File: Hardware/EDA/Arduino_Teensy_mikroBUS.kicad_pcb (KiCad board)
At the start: 4 copper layers, 38.1 x 69.8 mm, 32 parts, among them J1 HEADER_F_2.54MM_1R8P_ST_AU_PTH, J2 HEADER_F_2.54MM_1R8P_ST_AU_PTH, J3 HEADER_F_2.54MM_1R11P_ST_AU_P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, J3 Val**, J4 HEADER_F_2.54MM_1R11P_ST_AU_P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, J4 Val**, J5 Molex_0475710001, M1 FID, M2 FID, M3 FID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

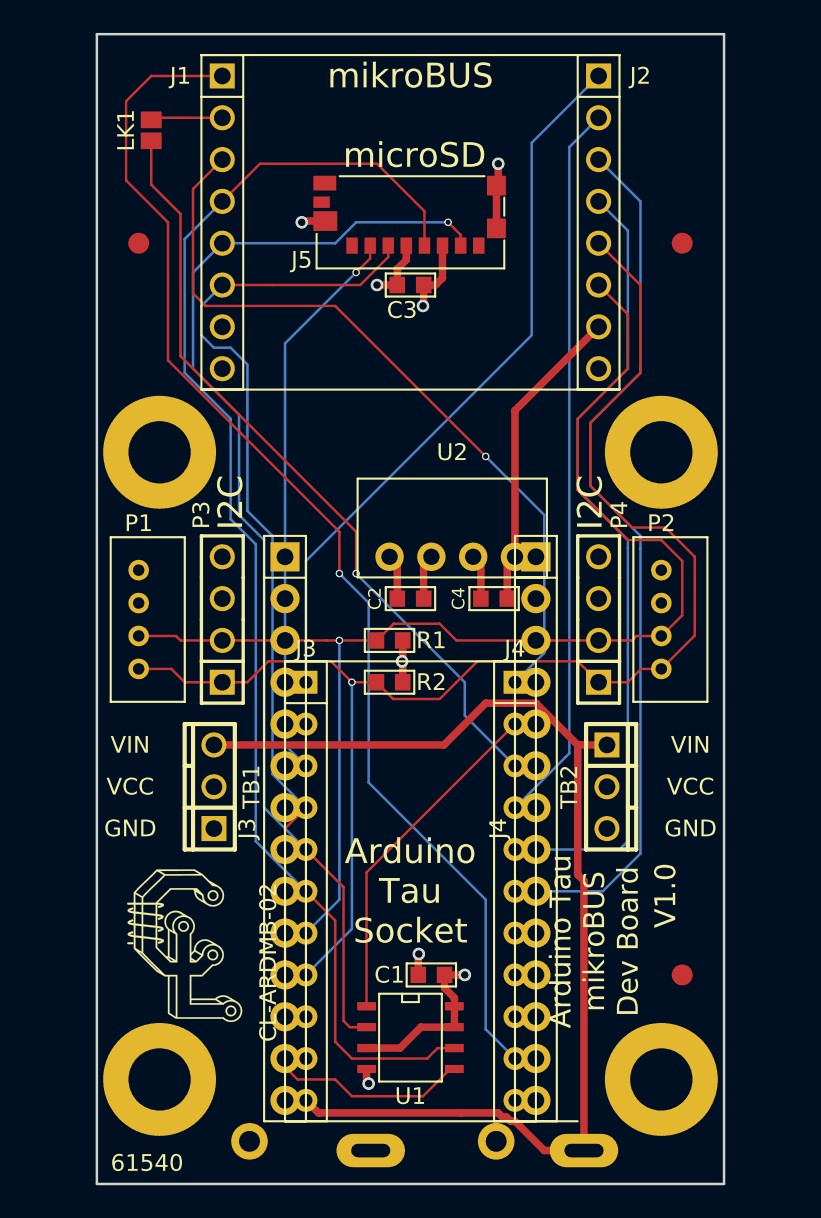
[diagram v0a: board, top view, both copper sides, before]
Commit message: Updated schematic, netlist and read in netlist to PCB file.  Added pinouts for Teensy.
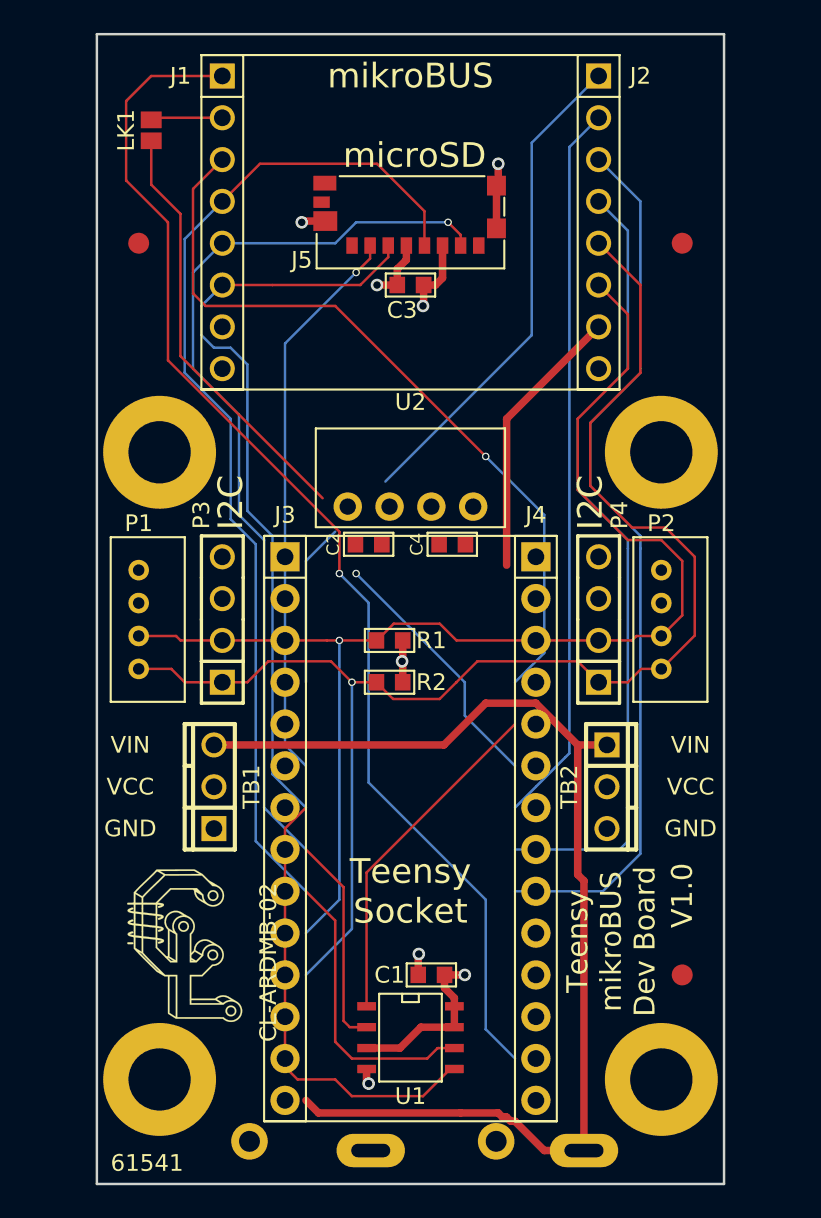
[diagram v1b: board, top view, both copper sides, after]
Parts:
- removed the J3 at (73.7, 83.8)
- removed the J4 at (86.4, 83.8)
- J3, J4: value Val** -> HEADER_F_2.54MM_1R14P_ST_AU_PTH
- moved C2 4.17 mm to (77.5, 62.7)
- moved C4 4.17 mm to (82.5, 62.7)
- moved U2 3.97 mm to (80.0, 60.5)
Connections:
- J2 pad 3: RXD -> RX1
- J2 pad 4: TXD -> TX1
- J3 pad 1: (no net) -> SCK
- J3 pad 10: (no net) -> A8
- J3 pad 11: (no net) -> A9
- J3 pad 12: (no net) -> 3V3
- J3 pad 13: (no net) -> GND
- J3 pad 14: (no net) -> VIN
- J3 pad 2: (no net) -> A0
- J3 pad 3: (no net) -> A1
- J3 pad 4: (no net) -> A2
- J3 pad 5: (no net) -> A3
- J3 pad 6: (no net) -> SDA
- J3 pad 7: (no net) -> SCL
- J3 pad 8: (no net) -> A6
- J3 pad 9: (no net) -> A7
- J4 pad 1: (no net) -> MISO
- J4 pad 10: (no net) -> D3
- J4 pad 11: (no net) -> D2
- J4 pad 12: (no net) -> TX1
- J4 pad 13: (no net) -> RX1
- J4 pad 14: (no net) -> GND
- J4 pad 2: (no net) -> MOSI
- J4 pad 3: (no net) -> D10
- J4 pad 4: (no net) -> D9
- J4 pad 5: (no net) -> D8
- J4 pad 6: (no net) -> D7
- J4 pad 7: (no net) -> D6
- J4 pad 8: (no net) -> D5
- J4 pad 9: (no net) -> D4
- J5 pad 1: (no net) -> Net-(J5-Pad1)
- J5 pad 12: (no net) -> Net-(J5-Pad12)
- J5 pad 13: (no net) -> Net-(J5-Pad13)
- J5 pad 2: D10 -> D6
- J5 pad 8: (no net) -> Net-(J5-Pad8)
- M1 pad ~: (no net) -> Net-(M1-Pad~)
- M2 pad ~: (no net) -> Net-(M2-Pad~)
- M3 pad ~: (no net) -> Net-(M3-Pad~)
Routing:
- net RXD: track 54.3 -> 0.00 mm
- net RX1: track 0.00 -> 54.3 mm
- net TXD: track 49.2 -> 0.00 mm
- net TX1: track 0.00 -> 49.2 mm
- net D6: track 0.00 -> 34.3 mm, vias 0 -> 1
- net D10: track 34.3 -> 0.00 mm, vias 1 -> 0
- net (no net): track 0.00 -> 25.6 mm, vias 0 -> 1
- net MOSI: track 75.0 -> 49.6 mm
- net D3: track 47.1 -> 26.0 mm, vias 1 -> 0
- net GND: track 17.7 -> 37.7 mm
- net D8: track 44.2 -> 30.0 mm
- net 3V3: track 19.7 -> 16.9 mm
- net 5.0V: track 18.8 -> 16.8 mm
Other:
- board text added: "61541"
- board text added: "Teensy Socket"
- board text added: "Teensy mikroBUS Dev Board"
- board text removed: "61540"
- board text removed: "Arduino Tau Socket"
- board text removed: "Arduino Tau mikroBUS Dev Board"

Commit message: Completed PCB layout, added PCB render image, generated gerbers and schematic.
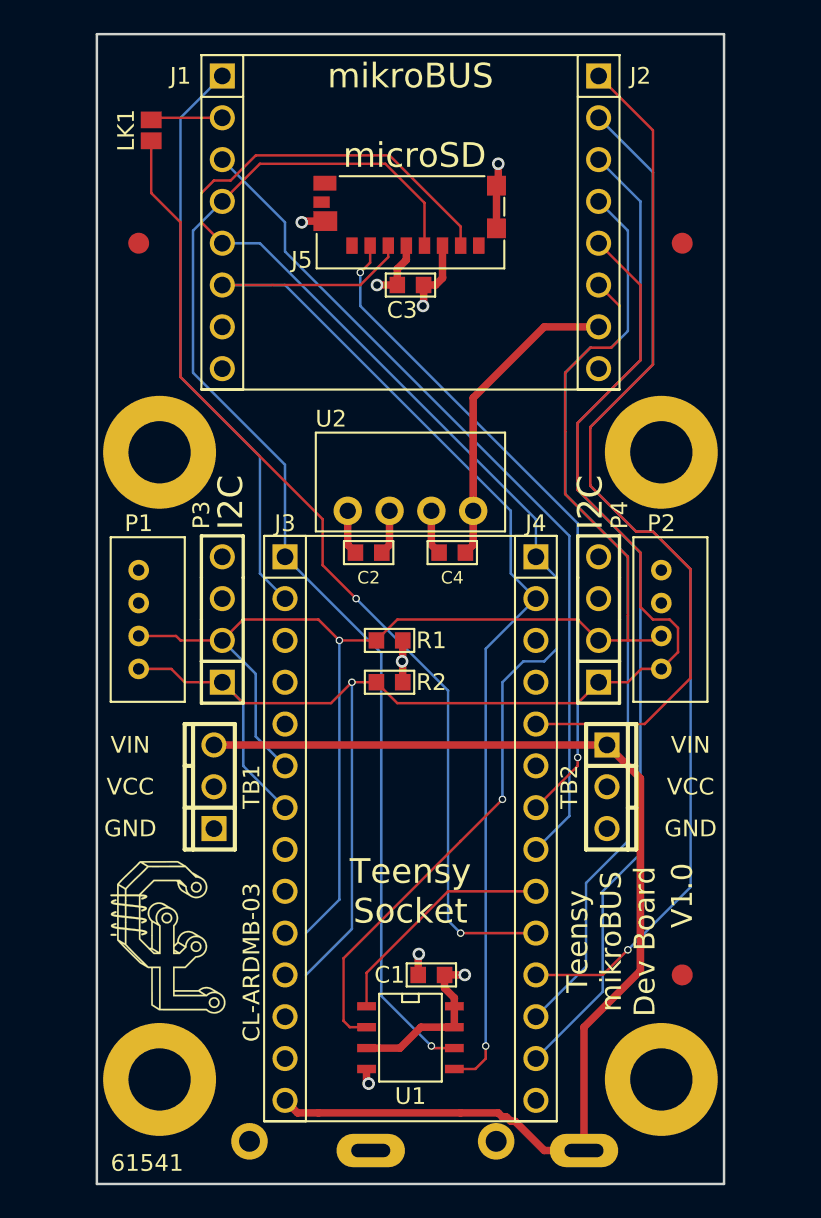
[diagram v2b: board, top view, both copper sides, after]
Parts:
- moved G1 1.14 mm to (65.3, 86.6)
- moved C2 0.51 mm to (77.5, 63.2)
- moved C4 0.51 mm to (82.5, 63.2)
- moved U2 0.25 mm to (80.0, 60.7)
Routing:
- net A0: track 74.4 -> 35.4 mm, vias 1 -> 0
- net D3: track 26.0 -> 60.5 mm, vias 0 -> 2
- net (no net): track 25.6 -> 0.00 mm, vias 1 -> 0
- net D8: track 30.0 -> 53.2 mm
- net MOSI: track 49.6 -> 72.3 mm, vias 0 -> 1
- net D2: track 44.0 -> 64.4 mm, vias 0 -> 1
- net GND: track 37.7 -> 17.7 mm
- net MISO: track 69.8 -> 88.4 mm
- net SDA: track 79.1 -> 87.7 mm
- net SCL: track 87.1 -> 94.7 mm
- net TX1: track 49.2 -> 56.5 mm
- net RX1: track 54.3 -> 61.4 mm
- net D6: track 34.3 -> 40.9 mm, vias 1 -> 2
- net D4: track 20.9 -> 14.4 mm
- net D5: track 46.7 -> 51.5 mm, vias 1 -> 0
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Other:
- board text added: "CL-ARDMB-03"
- board text removed: "CL-ARDMB-02"

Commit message: Changed PCB outline/size to accomodate mounting holes, but still fit in enclosure. Regenerated Gerbers and PCB render images.
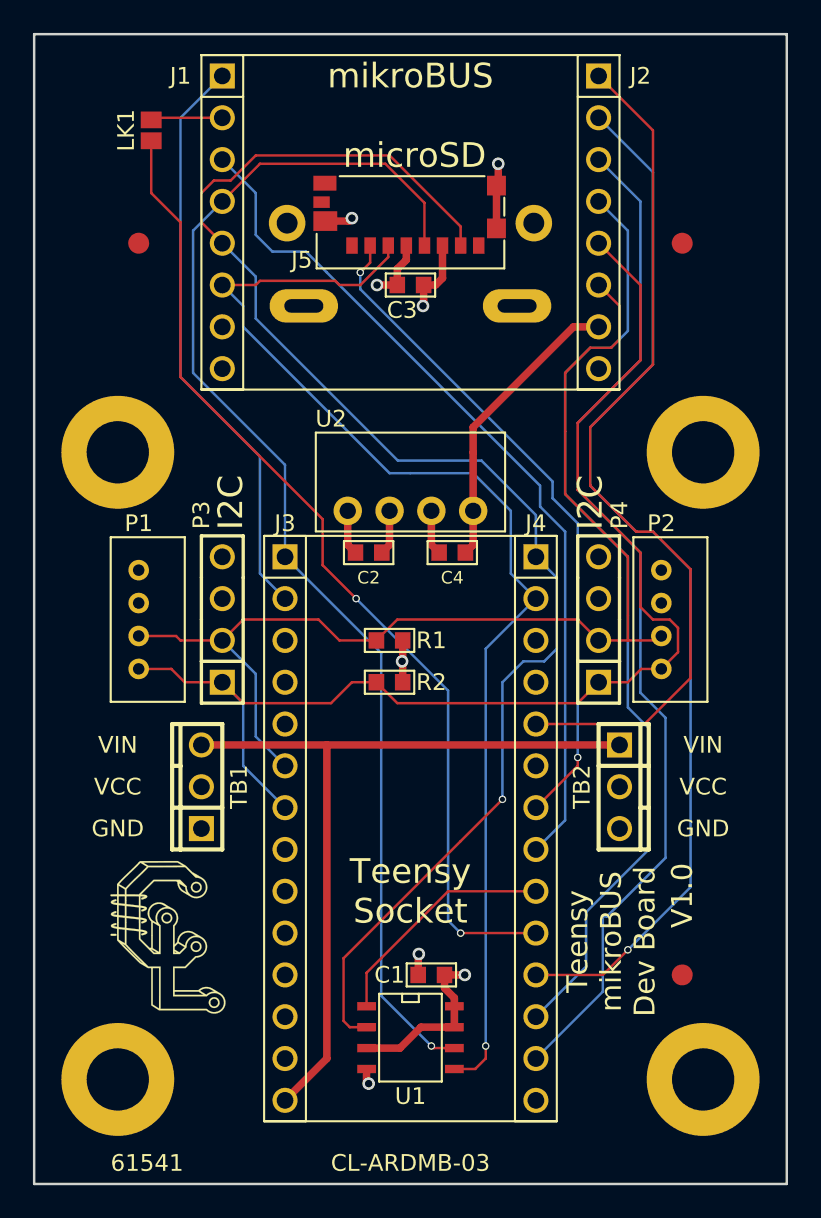
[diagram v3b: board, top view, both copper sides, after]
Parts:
- moved B1 51.5 mm to (80.0, 48.3), turned to 270 degrees
- moved MH2 2.54 mm to (97.8, 57.1)
- moved MH4 2.54 mm to (97.8, 95.2)
- moved MH1 2.54 mm to (62.2, 57.1)
- moved MH3 2.54 mm to (62.2, 95.2)
- moved B2 2.29 mm to (80.0, 71.1), turned to 90 degrees
- moved TB1 0.76 mm to (67.3, 77.5)
- moved TB2 0.76 mm to (92.7, 77.5)
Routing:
- net SCL: track 94.7 -> 75.8 mm, vias 1 -> 0
- net SDA: track 87.7 -> 69.1 mm, vias 1 -> 0
- net VIN: track 70.2 -> 77.3 mm
- net MISO: track 88.4 -> 90.0 mm
- net RX1: track 61.4 -> 62.9 mm
- net TX1: track 56.5 -> 57.5 mm
- net 5.0V: track 19.0 -> 18.0 mm
- net D5: track 51.5 -> 52.5 mm
- net MOSI: track 72.3 -> 73.2 mm
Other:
- board size 38.1 x 69.8 mm -> 45.7 x 69.8 mm

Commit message: Adjustment of mounting hole locations was missed. Corrected and updated gerbers and dimensions.
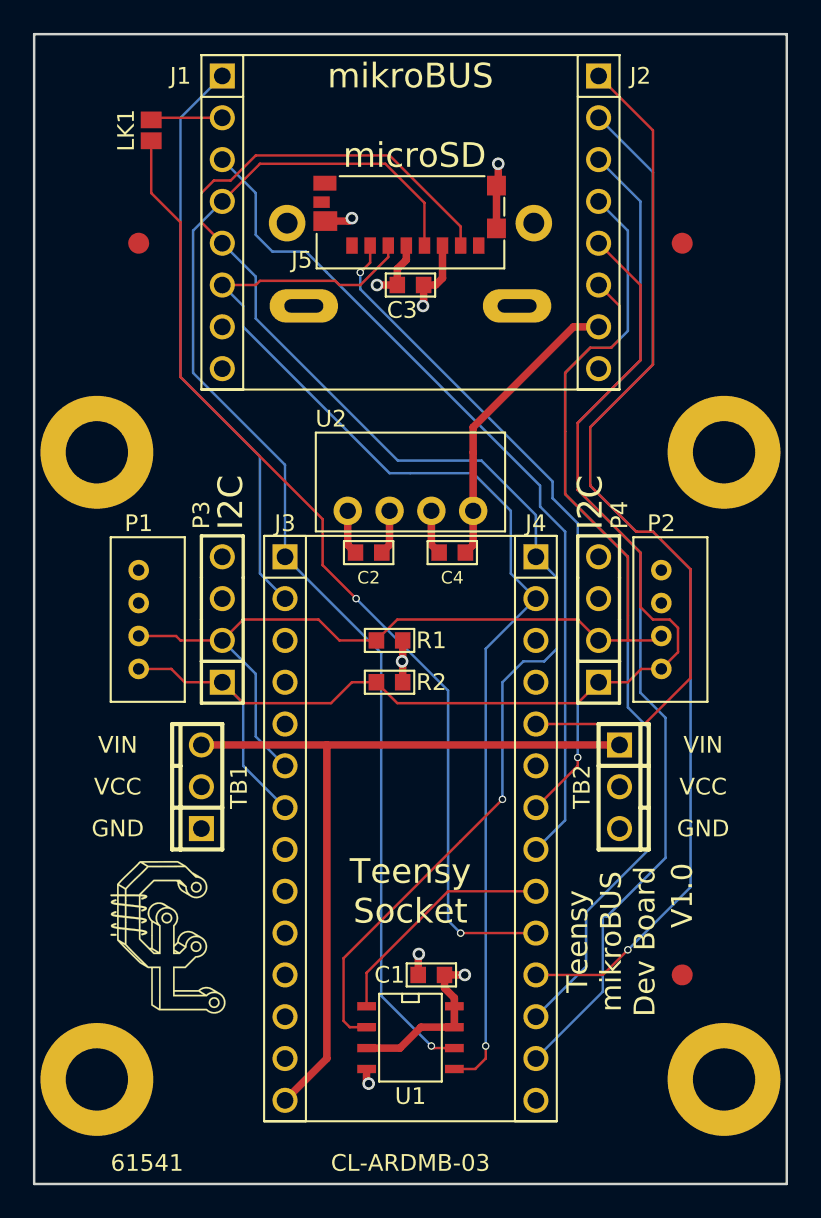
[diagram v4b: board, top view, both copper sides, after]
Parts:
- moved MH1 1.27 mm to (61.0, 57.1)
- moved MH2 1.27 mm to (99.1, 57.1)
- moved MH3 1.27 mm to (61.0, 95.2)
- moved MH4 1.27 mm to (99.1, 95.2)
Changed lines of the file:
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@@
       (net 36 "Net-(M3-Pad~)") (solder_mask_margin 0.635) (clearance 0.635))
   )
-  (module Fastener:MH_#6 (layer F.Cu)
-    (at 62.23 57.15)
+  (module Fastener:MH_#6 locked (layer F.Cu)
+    (at 60.96 57.15)
     (fp_text reference MH1 (at 0 4.445) (layer F.SilkS) hide
       (effects (font (size 1 1) (thickness 0.15)))
@@
       (net 1 GND))
   )
-  (module Fastener:MH_#6 (layer F.Cu)
-    (at 97.79 57.15)
+  (module Fastener:MH_#6 locked (layer F.Cu)
+    (at 99.06 57.15)
     (fp_text reference MH2 (at 0 4.445) (layer F.SilkS) hide
       (effects (font (size 1 1) (thickness 0.15)))
@@
       (net 1 GND))
   )
-  (module Fastener:MH_#6 (layer F.Cu)
-    (at 62.23 95.25)
+  (module Fastener:MH_#6 locked (layer F.Cu)
+    (at 60.96 95.25)
     (fp_text reference MH3 (at -1.524 -4.318) (layer F.SilkS) hide
       (effects (font (size 1 1) (thickness 0.15)))
@@
       (net 1 GND))
   )
-  (module Fastener:MH_#6 (layer F.Cu)
-    (at 97.79 95.25)
+  (module Fastener:MH_#6 locked (layer F.Cu)
+    (at 99.06 95.25)
     (fp_text reference MH4 (at 1.778 -4.318) (layer F.SilkS) hide
       (effects (font (size 1 1) (thickness 0.15)))
@@
     )
   )
+  (dimension 41.91 (width 0.3) (layer Dwgs.User)
+    (gr_text "1.6500 in" (at 78.105 111.84) (layer Dwgs.User)
+      (effects (font (size 1.5 1.5) (thickness 0.3)))
+    )
+    (feature1 (pts (xy 99.06 102.87) (xy 99.06 113.19)))
+    (feature2 (pts (xy 57.15 102.87) (xy 57.15 113.19)))
+    (crossbar (pts (xy 57.15 110.49) (xy 99.06 110.49)))
+    (arrow1a (pts (xy 99.06 110.49) (xy 97.933496 111.076421)))
+    (arrow1b (pts (xy 99.06 110.49) (xy 97.933496 109.903579)))
+    (arrow2a (pts (xy 57.15 110.49) (xy 58.276504 111.076421)))
+    (arrow2b (pts (xy 57.15 110.49) (xy 58.276504 109.903579)))
+  )
+  (dimension 3.81 (width 0.3) (layer Dwgs.User)
+    (gr_text "0.1500 in" (at 67.31 105.41) (layer Dwgs.User)
+      (effects (font (size 1.5 1.5) (thickness 0.3)))
+    )
+    (feature1 (pts (xy 60.96 102.87) (xy 60.96 108.11)))
+    (feature2 (pts (xy 57.15 102.87) (xy 57.15 108.11)))
+    (crossbar (pts (xy 57.15 105.41) (xy 60.96 105.41)))
+    (arrow1a (pts (xy 60.96 105.41) (xy 59.833496 105.996421)))
+    (arrow1b (pts (xy 60.96 105.41) (xy 59.833496 104.823579)))
+    (arrow2a (pts (xy 57.15 105.41) (xy 58.276504 105.996421)))
+    (arrow2b (pts (xy 57.15 105.41) (xy 58.276504 104.823579)))
+  )
   (dimension 45.72 (width 0.3) (layer Dwgs.User)
     (gr_text "1.8000 in" (at 80.01 26.59) (layer Dwgs.User)
@@
   (gr_line (start 57.15 31.75) (end 102.87 31.75) (angle 90) (layer Edge.Cuts) (width 0.15))
   (gr_line (start 57.15 101.6) (end 102.87 101.6) (angle 90) (layer Edge.Cuts) (width 0.15))
-  (dimension 40.64 (width 0.3) (layer Dwgs.User)
-    (gr_text "1.6000 in" (at 77.47 111.84) (layer Dwgs.User)
-      (effects (font (size 1.5 1.5) (thickness 0.3)))
-    )
-    (feature1 (pts (xy 97.79 102.87) (xy 97.79 113.19)))
-    (feature2 (pts (xy 57.15 102.87) (xy 57.15 113.19)))
-    (crossbar (pts (xy 57.15 110.49) (xy 97.79 110.49)))
-    (arrow1a (pts (xy 97.79 110.49) (xy 96.663496 111.076421)))
-    (arrow1b (pts (xy 97.79 110.49) (xy 96.663496 109.903579)))
-    (arrow2a (pts (xy 57.15 110.49) (xy 58.276504 111.076421)))
-    (arrow2b (pts (xy 57.15 110.49) (xy 58.276504 109.903579)))
-  )
-  (dimension 5.08 (width 0.3) (layer Dwgs.User)
-    (gr_text "0.2000 in" (at 68.58 105.41) (layer Dwgs.User)
-      (effects (font (size 1.5 1.5) (thickness 0.3)))
-    )
-    (feature1 (pts (xy 62.23 102.87) (xy 62.23 108.11)))
-    (feature2 (pts (xy 57.15 102.87) (xy 57.15 108.11)))
-    (crossbar (pts (xy 57.15 105.41) (xy 62.23 105.41)))
-    (arrow1a (pts (xy 62.23 105.41) (xy 61.103496 105.996421)))
-    (arrow1b (pts (xy 62.23 105.41) (xy 61.103496 104.823579)))
-    (arrow2a (pts (xy 57.15 105.41) (xy 58.276504 105.996421)))
-    (arrow2b (pts (xy 57.15 105.41) (xy 58.276504 104.823579)))
-  )
   (dimension 44.45 (width 0.3) (layer Dwgs.User)
     (gr_text "1.7500 in" (at 46.91 79.375 90) (layer Dwgs.User)
@@
   (segment (start 83.82 60.706) (end 83.82 57.15) (width 0.4572) (layer F.Cu) (net 9))
   (segment (start 83.82 55.626) (end 89.916 49.53) (width 0.4572) (layer F.Cu) (net 9))
-  (segment (start 89.916 49.53) (end 91.44 49.53) (width 0.4572) (layer F.Cu) (net 9) (status 800000))
+  (segment (start 89.916 49.53) (end 91.44 49.53) (width 0.4572) (layer F.Cu) (net 9))
   (segment (start 83.82 57.15) (end 83.82 55.626) (width 0.4572) (layer F.Cu) (net 9))
   (segment (start 83.35 63.246) (end 83.82 62.776) (width 0.4572) (layer F.Cu) (net 9))

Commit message: Added comments to PCB file to indicate updates needed.
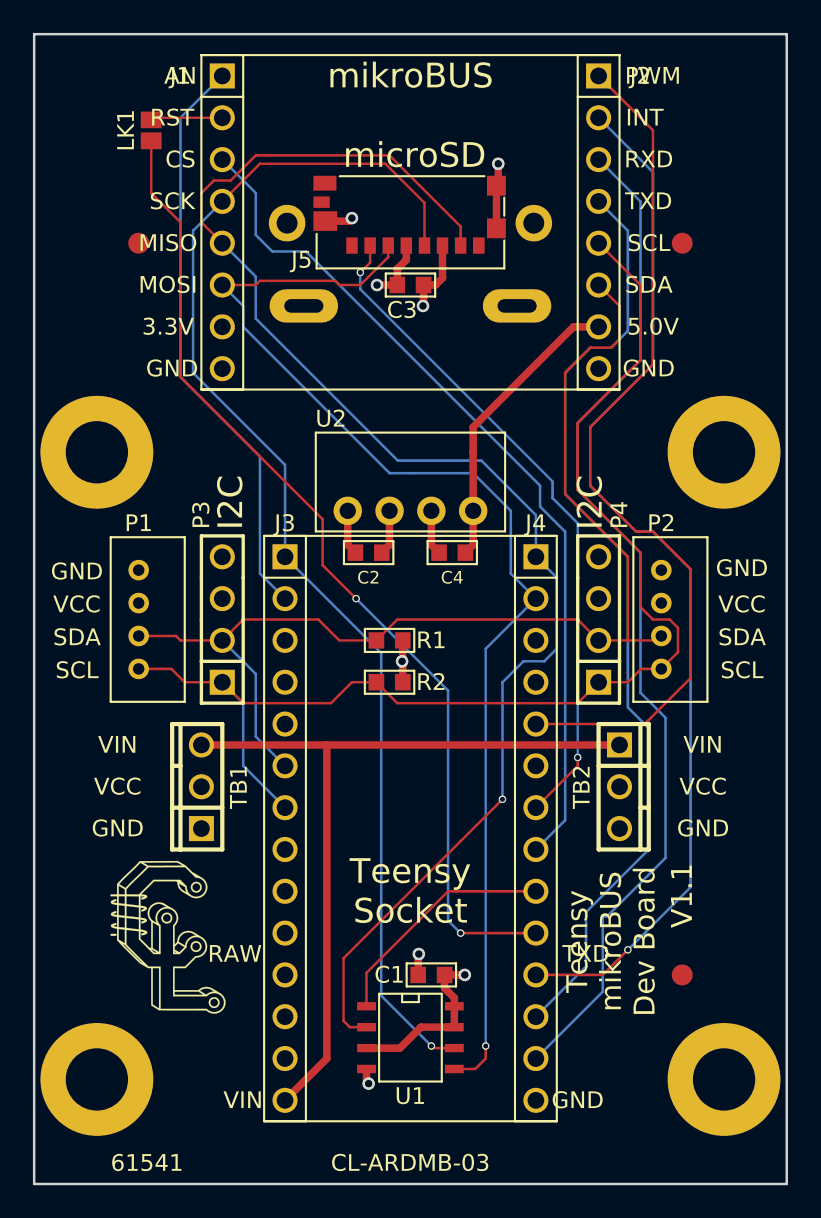
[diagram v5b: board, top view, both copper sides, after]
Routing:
- net VIN: track 77.3 -> 84.4 mm
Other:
- board text added: "3.3V"
- board text added: "5.0V"
- board text added: "AN"
- board text added: "CS"
- board text added: "Corrections made:"
- board text added: "Corrections needed: RTC needs crystal and caps Add silkscreen pin names to mikroBUS connector Check FL127 footprint against Winbond footprint Add level shifter for microSD socket? Corrected pin numbering of 2xAA battery holder footprint to match schematic decal Corrected pin numbering of 1x9V battery holder footprint to match schematic decal Re-layed out 2xAA battery traces Re-layed out 1x9V batt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"
- board text added: "INT"
- board text added: "MISO"
- board text added: "MOSI"
- board text added: "PWM"
- board text added: "RAW"
- board text added: "RST"
- board text added: "RXD"
- board text added: "SCK"
- board text added: "SCL"
- board text added: "SDA"
- board text added: "TXD"
- board text added: "V1.1"
- board text removed: "V1.0"
